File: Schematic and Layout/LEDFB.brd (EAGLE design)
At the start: 160 x 100 mm, 25 parts, among them U1 TLV61225L

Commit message: Changed stuff
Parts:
- added C3: 10uF, adafruit:C0805
- added R11, R12: 4.7k, adafruit:M0805
- added U$7: LQH3NPN4R7NJ0, inductor:1212
- added U2: ITG-37013X3MM, itg_3701:QFN-16
- R10, R4, R8, R9: value (none) -> 60
- R2, R3: value (none) -> 300
- U1: value TLV61225L -> TLV61225M; device TLV61225:DCK0006A_L -> TLV61225:DCK0006A_M
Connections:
- removed net N$10: U$3.3
- removed net N$11: U$4.3
- removed net VIN: U1.1
- removed net VOUT: U1.4
- new net INT: U$1.6, U2.10
- new net N$21: S2.P, U1.6
- new net N$22: U$7.P$2, U1.5
- new net NC3: U2.13
- new net NC4: U2.15
- new net NC_RSVD: U2.5
- new net SCL: R12.1, U$1.14, U2.16
- new net SDA: R11.1, U$1.15, U2.1
- net GND: now also C3.2, S2.O, U$3.3, U$4.3, U2.12, U2.14, U2.6, U2.8
- net GREEN_CTRL: now also U$1.12
- net N$17: now also U$4.2
- net N$20: now also S2.S, U$7.P$1, U1.1
- net VCC: now also C3.1, R11.2, R12.2, U1.2, U1.4, U2.3, U2.4, U2.9

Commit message: Completed first rev of layout
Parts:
- removed BATT1: AAA, adafruit:12BH412
- removed S1: (no value), switch-omron:B3F-10XX
- removed U$1: G2XX3---PW20, TI_MSP430_v16:PW20
- removed U$2, U$3, U$4: MMBT3904FSCT-ND, GuShH:SOT-23
- removed U$5, U$6: LED_PIRANHA_5MM, SparkFun-LED:LED_PIRANHA_5MM
- removed U$7: LQH3NPN4R7NJ0, inductor:1212
- removed U1: TLV61225M, TLV61225:DCK0006A_M
- added AAA: AAA, adafruit:12BH412
- added H1, H2, H3, H4: STAND-OFF, SparkFun-Electromechanical:STAND-OFF
- added RST: (no value), switch-omron:B3F-10XX
- added U1\: G2XX3---PW20, TI_MSP430_v16:PW20
- added U3: LED_PIRANHA_5MM, SparkFun-LED:LED_PIRANHA_5MM
- added U4, U5, U6: MMBT3904FSCT-ND, GuShH:SOT-23
- added U7: ITG-37013X3MM, itg_3701:QFN-16
- added U8: LQH3NPN4R7NJ0, inductor:1212
- added U9: TLV61225M, TLV61225:DCK0006A_M
- JP2: device pinhead:1X02 -> pinhead:1X03
- R10, R8, R9: value 60 -> 10
- R5, R6, R7: value 10 -> 60
- U2: value ITG-37013X3MM -> LED_PIRANHA_5MM; device itg_3701:QFN-16 -> SparkFun-LED:LED_PIRANHA_5MM
- moved R12 108.3 mm to (27.9, 30.2), turned to 180 degrees
- moved R11 104.9 mm to (27.9, 27.6), turned to 180 degrees
- moved JP2 104.5 mm to (60.8, 41.0), turned to 90 degrees
- moved R5 101.7 mm to (60.0, 17.0), turned to 270 degrees
- moved C3 97.2 mm to (24.3, 24.3), turned to 270 degrees
- moved R10 93.7 mm to (41.3, 8.10), turned to 180 degrees
- moved R7 81.7 mm to (63.7, 17.0), turned to 270 degrees
- moved R3 80.6 mm to (56.4, 17.0), turned to 270 degrees
- moved C1 79.0 mm to (48.1, 23.7)
- moved JP3 77.3 mm to (60.8, 32.4), turned to 270 degrees
- moved R9 74.6 mm to (31.0, 8.10), turned to 180 degrees
- moved R1 63.5 mm to (27.9, 32.5), turned to 180 degrees
- moved JP1 63.1 mm to (42.7, 34.8)
- moved R8 61.4 mm to (20.8, 8.10), turned to 180 degrees
- moved R6 56.1 mm to (8.26, 16.5), turned to 270 degrees
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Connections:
- net BLUE_CTRL: now also R9.2, U1\.9; no longer R6.2, U$1.9
- net GND: now also AAA.-, JP2.1, RST.1, RST.2, U1\.18, U1\.19, U1\.20, U4.2, U5.2, U6.2, U7.12, U7.14, U7.6, U7.8, U9.3; no longer BATT1.+, S1.1, S1.2, U$1.20, U$2.3, U$3.3, U$4.3, U1.3, U2.12, U2.14, U2.6, U2.8
- net GREEN_CTRL: now also R10.2, U1\.12; no longer R7.2, U$1.12
- net INT: now also U1\.6, U7.10; no longer U$1.6, U2.10
- net N$1: now also U1\.3; no longer U$1.3
- net N$12: now also R8.1, U4.1; no longer R5.1, U$2.1
- net N$13: now also R9.1, U5.1; no longer R6.1, U$3.1
- net N$14: now also R10.1, U6.1; no longer R7.1, U$4.1
- net N$15: now also R5.1, U3.B; no longer R8.1, U$6.B
- net N$16: now also R5.2, U5.3; no longer R8.2, U$3.2
- net N$17: now also R6.2, R7.2, U6.3; no longer R10.2, R9.2, U$4.2
- net N$18: now also R6.1, U2.G; no longer R9.1, U$5.G
- net N$19: now also R7.1, U3.G; no longer R10.1, U$6.G
- net N$2: now also U1\.4; no longer U$1.4
- net N$20: now also AAA.+, U8.P$1, U9.1; no longer BATT1.-, U$7.P$1, U1.1
- net N$21: now also U9.6; no longer U1.6
- net N$22: now also U8.P$2, U9.5; no longer U$7.P$2, U1.5
- net N$3: now also U1\.13; no longer U$1.13
- net N$4: now also U2.R; no longer U$5.R
- net N$5: now also U3.R; no longer U$6.R
- net N$6: now also JP2.2, U1\.17; no longer JP2.1, U$1.17
- net N$7: now also JP2.3, RST.3, RST.4, U1\.16; no longer JP2.2, S1.3, S1.4, U$1.16
- net N$8: now also U4.3; no longer U$2.2
- net N$9: now also U2.B; no longer U$5.B
- net NC3: now also U7.13; no longer U2.13
- net NC4: now also U7.15; no longer U2.15
- net NC_RSVD: now also U7.5; no longer U2.5
- net RED_CTRL: now also R8.2, U1\.10; no longer R5.2, U$1.10
- net SCL: now also U1\.14, U7.16; no longer U$1.14, U2.16
- net SDA: now also U1\.15, U7.1; no longer U$1.15, U2.1
- net VCC: now also U1\.1, U2.C, U3.C, U7.3, U7.4, U7.9, U9.2, U9.4; no longer U$1.1, U$5.C, U$6.C, U1.2, U1.4, U2.3, U2.4, U2.9
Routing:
- net VCC: track 0.00 -> 79.7 mm
- net N$17: track 0.00 -> 72.5 mm, vias 0 -> 2
- net N$8: track 0.00 -> 65.3 mm, vias 0 -> 2
- net RED_CTRL: track 0.00 -> 59.6 mm, vias 0 -> 2
- net N$16: track 0.00 -> 55.3 mm
- net BLUE_CTRL: track 0.00 -> 55.0 mm, vias 0 -> 2
- net N$7: track 0.00 -> 44.4 mm, vias 0 -> 2
- net N$20: track 0.00 -> 36.4 mm, vias 0 -> 2
- net N$6: track 0.00 -> 26.6 mm
- net GREEN_CTRL: track 0.00 -> 25.3 mm, vias 0 -> 2
- net N$21: track 0.00 -> 21.7 mm, vias 0 -> 1
- net N$2: track 0.00 -> 16.2 mm
- net SDA: track 0.00 -> 15.7 mm, vias 0 -> 2
- net N$1: track 0.00 -> 15.4 mm
- net SCL: track 0.00 -> 15.2 mm
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- added copper zone on layer 1, net GND
- added copper zone on layer 16, net GND
- added copper zone on layer 16, net N$10
- added copper zone on layer 1, net N$20
- added copper zone on layer 1, net N$22
- added copper zone on layer 1, net VCC
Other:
- board size 160 x 100 mm -> 69.8 x 50.8 mm
- board text added: "GND"
- board text added: "GPIO"
- board text added: "OFF"
- board text added: "ON"
- board text added: "RST"
- board text added: "RXD"
- board text added: "TEST"
- board text added: "TXD"

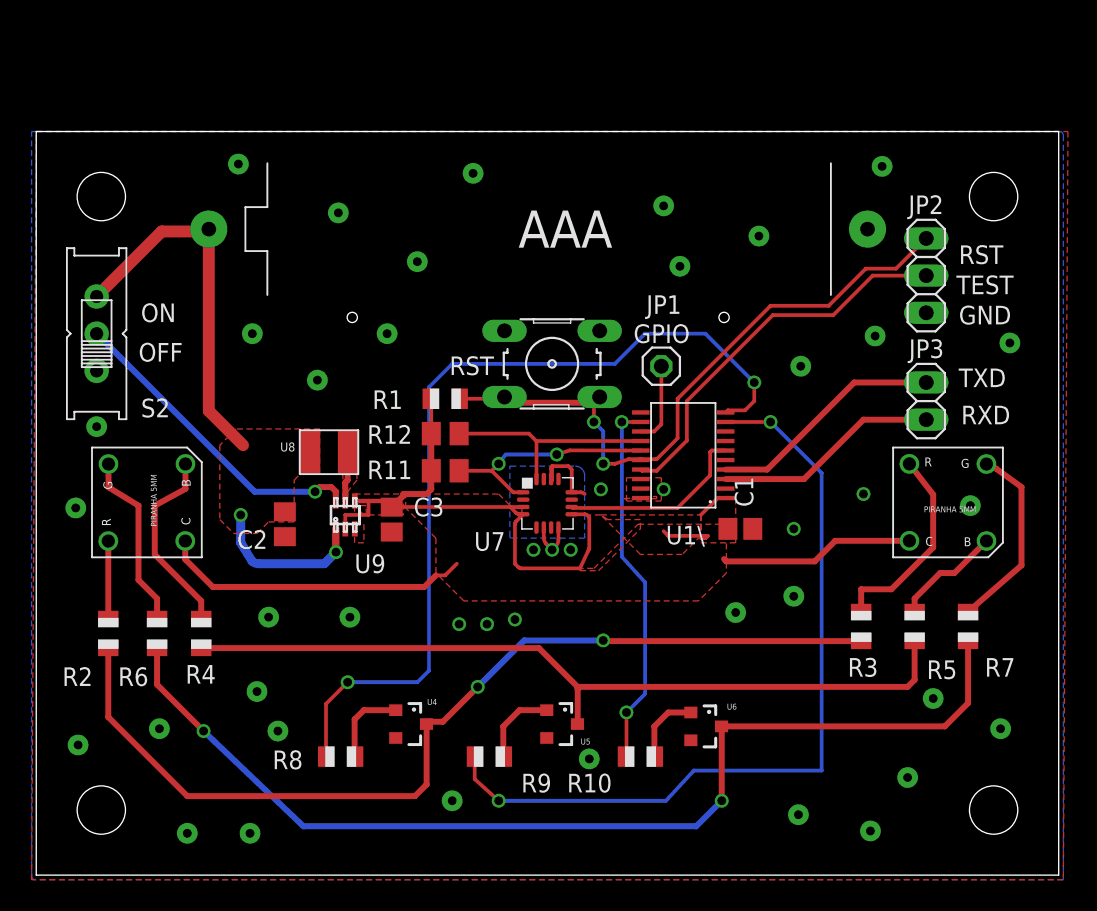
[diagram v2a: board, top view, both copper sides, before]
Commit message: Increased board size to accomidate battery holder size and added standoffs. Generated a BOM.
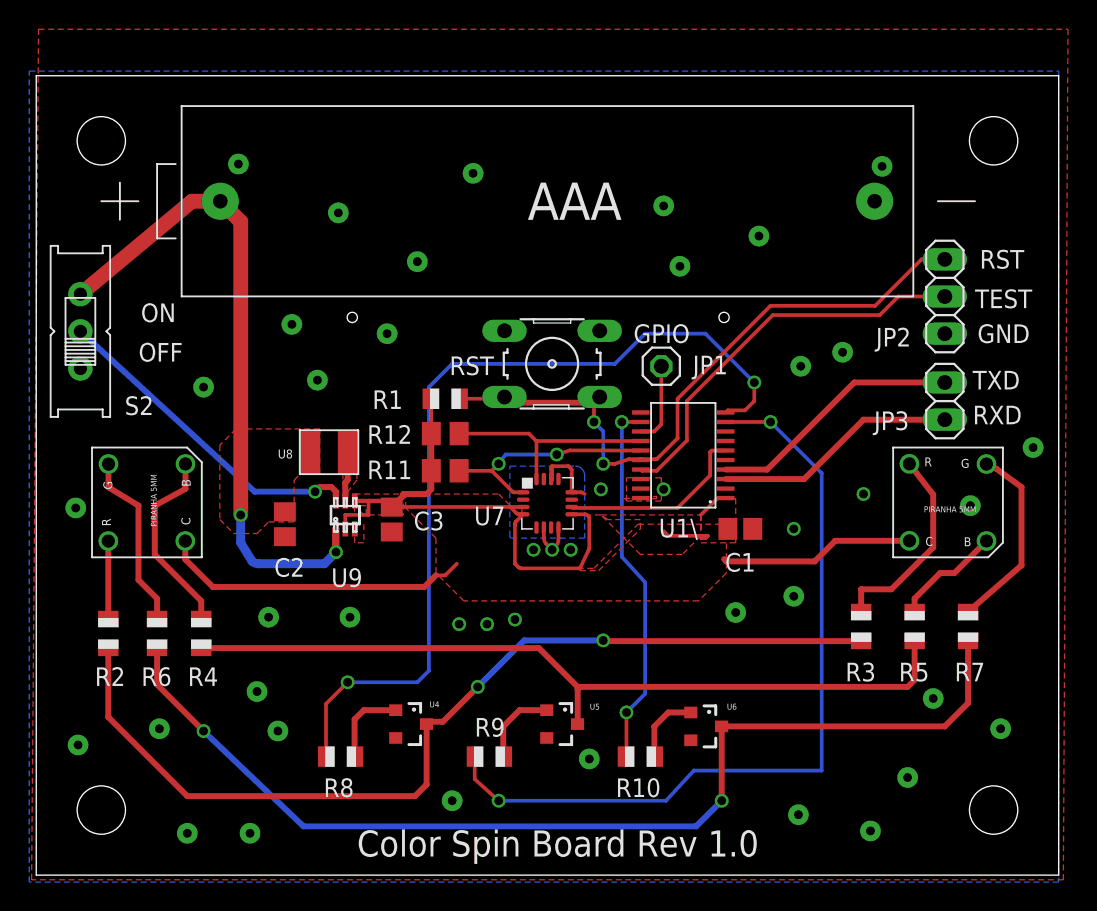
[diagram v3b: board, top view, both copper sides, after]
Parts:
- moved H3 3.81 mm to (4.45, 50.2)
- moved H4 3.81 mm to (65.4, 50.2)
- moved AAA 2.01 mm to (34.9, 46.0)
- moved JP2 1.91 mm to (62.1, 39.5)
- moved JP3 1.27 mm to (62.1, 32.4)
- moved S2 1.12 mm to (3.02, 37.1)
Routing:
- net N$20: track 36.4 -> 44.9 mm
- net N$2: track 16.2 -> 17.4 mm
- net N$1: track 15.4 -> 16.6 mm
- net N$21: track 21.7 -> 22.6 mm
- net N$7: track 44.4 -> 45.0 mm
- net N$6: track 26.6 -> 27.3 mm
- added copper zone on layer 16, net N$11
- removed copper zone on layer 16, net GND
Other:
- board size 69.8 x 50.8 mm -> 69.8 x 54.6 mm
- board text added: "Color Spin Board Rev 1.0"

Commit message: Fixed ground plane issue
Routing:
- added copper zone on layer 16, net GND
- removed copper zone on layer 16, net N$11
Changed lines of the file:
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@@
 <?xml version="1.0" encoding="utf-8"?>
 <!DOCTYPE eagle SYSTEM "eagle.dtd">
-<eagle version="7.5.0">
+<eagle version="6.5.0">
 <drawing>
 <settings>
@@
 <layer number="27" name="tValues" color="7" fill="1" visible="yes" active="yes"/>
 <layer number="28" name="bValues" color="7" fill="1" visible="yes" active="yes"/>
-<layer number="29" name="tStop" color="7" fill="3" visible="no" active="yes"/>
-<layer number="30" name="bStop" color="7" fill="6" visible="no" active="yes"/>
+<layer number="29" name="tStop" color="7" fill="3" visible="yes" active="yes"/>
+<layer number="30" name="bStop" color="7" fill="6" visible="yes" active="yes"/>
 <layer number="31" name="tCream" color="7" fill="4" visible="yes" active="yes"/>
 <layer number="32" name="bCream" color="7" fill="5" visible="yes" active="yes"/>
@@
 <pass name="Default">
 <param name="RoutingGrid" value="50mil"/>
-<param name="AutoGrid" value="1"/>
-<param name="Efforts" value="0"/>
-<param name="TopRouterVariant" value="1"/>
 <param name="tpViaShape" value="round"/>
-<param name="PrefDir.1" value="a"/>
+<param name="PrefDir.1" value="|"/>
 <param name="PrefDir.2" value="0"/>
 <param name="PrefDir.3" value="0"/>
@@
 <param name="PrefDir.14" value="0"/>
 <param name="PrefDir.15" value="0"/>
-<param name="PrefDir.16" value="a"/>
+<param name="PrefDir.16" value="-"/>
 <param name="cfVia" value="8"/>
 <param name="cfNonPref" value="5"/>
@@
 <via x="51.7525" y="23.65375" extent="1-16" drill="0.6"/>
 <via x="56.515" y="26.035" extent="1-16" drill="0.6"/>
-<wire x1="35.675" y1="23.745" x2="36.58" y2="26.15" width="0" layer="19" extent="1-1"/>
+<polygon width="0.4064" layer="16">
+<vertex x="-0.47625" y="54.9275"/>
+<vertex x="69.85" y="54.9275"/>
+<vertex x="69.85" y="-0.47625"/>
+<vertex x="-0.47625" y="-0.47625"/>
+</polygon>
 </signal>
 <signal name="N$1">
@@
 </polygon>
 </signal>
-<signal name="N$11">
-<polygon width="0.4064" layer="16">
-<vertex x="-0.47625" y="54.9275"/>
-<vertex x="69.85" y="54.9275"/>
-<vertex x="69.85" y="-0.47625"/>
-<vertex x="-0.47625" y="-0.47625"/>
-</polygon>
-</signal>

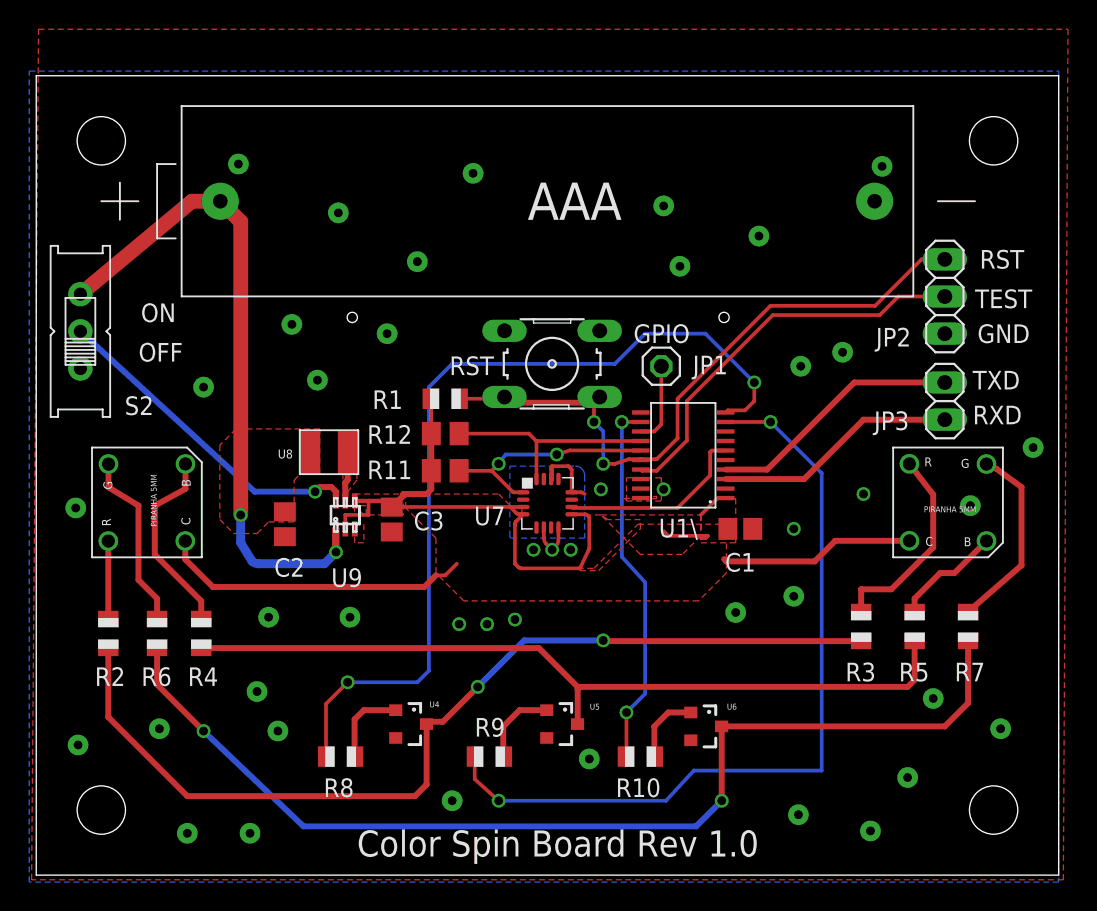
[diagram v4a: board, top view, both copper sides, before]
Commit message: Changed some spacings and sizes, removed some vias, and generated GERBERS
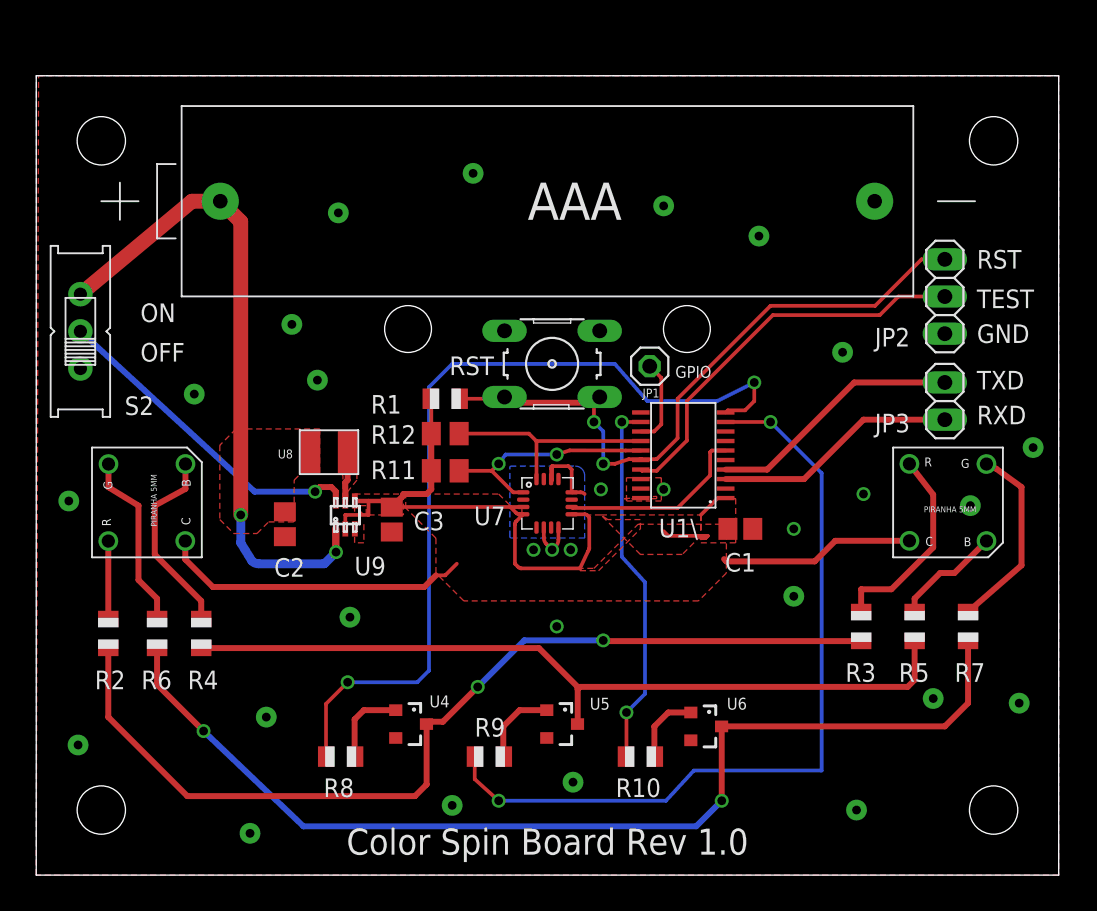
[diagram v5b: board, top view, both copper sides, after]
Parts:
- moved JP1 0.79 mm to (41.9, 34.8)
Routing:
- net RED_CTRL: track 59.6 -> 58.8 mm
- net GND: vias 44 -> 29
